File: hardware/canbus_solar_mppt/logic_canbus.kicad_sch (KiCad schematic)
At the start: 31 parts, among them J4 Conn_01x05_Male, J5 CANPWR, J6 CANGND, J7 RJ45, J8 RJ45, J9 Conn_02x03_Odd_Even, Q9 BSS123, U5 2.048V, U6 PIC18F27Q84, U7 TLE9250VSJXUMA1, Y1 10Mhz

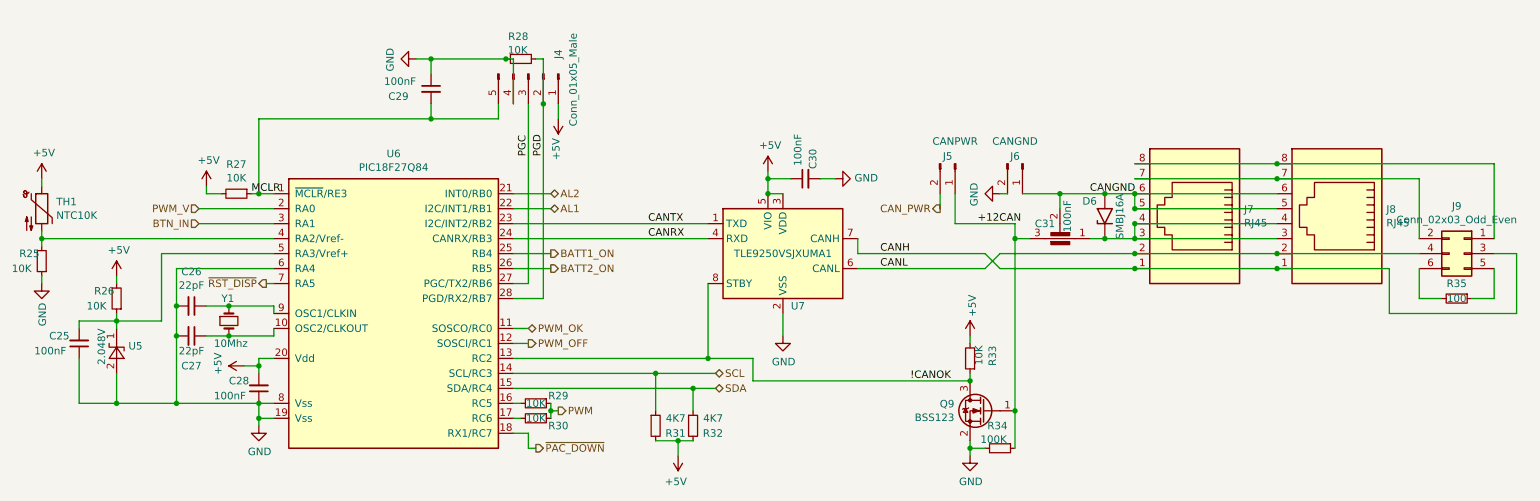
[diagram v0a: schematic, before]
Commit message: Switch from BSS123 + GS resistor to DGD0215 mosfet driver.
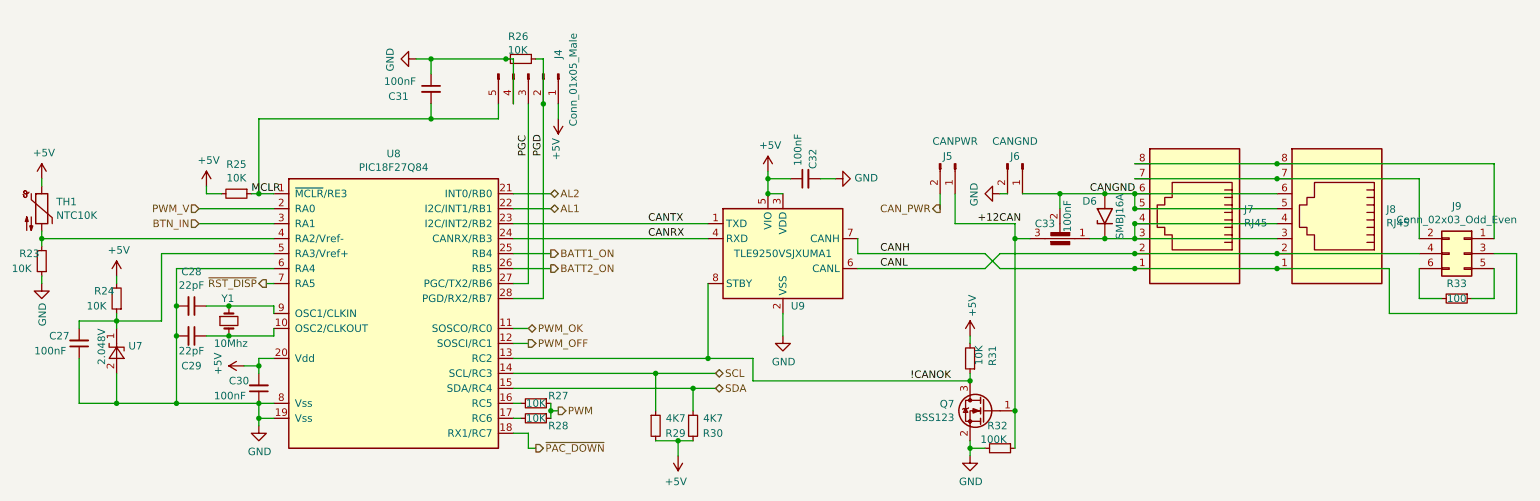
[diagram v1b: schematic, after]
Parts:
- renumbered C25 to C27, C26 to C28, C27 to C29, C28 to C30, C29 to C31, C30 to C32, C31 to C33, Q9 to Q7, R25 to R23, R26 to R24, R27 to R25, R28 to R26, R29 to R27, R30 to R28, R31 to R29, R32 to R30, R33 to R31, R34 to R32, R35 to R33, U5 to U7, U6 to U8, U7 to U9
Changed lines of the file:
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@@
   (symbol (lib_id "Device:Q_NMOS_GSD") (at 191.77 109.22 0) (mirror y) (unit 1)
     (in_bom yes) (on_board yes)
-    (property "Reference" "Q9" (id 0) (at 186.563 108.0516 0)
+    (property "Reference" "Q7" (id 0) (at 186.563 108.0516 0)
       (effects (font (size 1.27 1.27)) (justify left))
     )
@@
   (symbol (lib_id "Device:C_Small") (at 68.58 105.41 180) (unit 1)
     (in_bom yes) (on_board yes)
-    (property "Reference" "C28" (id 0) (at 63.5 104.14 0)
+    (property "Reference" "C30" (id 0) (at 63.5 104.14 0)
       (effects (font (size 1.27 1.27)) (justify right))
     )
@@
   (symbol (lib_id "Device:R_Small") (at 113.03 49.53 270) (unit 1)
     (in_bom yes) (on_board yes)
-    (property "Reference" "R28" (id 0) (at 114.3 45.72 90)
+    (property "Reference" "R26" (id 0) (at 114.3 45.72 90)
       (effects (font (size 1.27 1.27)) (justify right))
     )
@@
   (symbol (lib_id "Device:C_Feedthrough") (at 204.47 77.47 180) (unit 1)
     (in_bom yes) (on_board yes)
-    (property "Reference" "C31" (id 0) (at 201.93 77.47 0))
+    (property "Reference" "C33" (id 0) (at 201.93 77.47 0))
     (property "Value" "100nF" (id 1) (at 205.74 76.2 90))
     (property "Footprint" "local:C_filter_0805" (id 2) (at 204.47 77.47 90)
@@
   (symbol (lib_id "Device:C_Small") (at 97.79 54.61 0) (unit 1)
     (in_bom yes) (on_board yes)
-    (property "Reference" "C29" (id 0) (at 93.98 55.88 0)
+    (property "Reference" "C31" (id 0) (at 93.98 55.88 0)
       (effects (font (size 1.27 1.27)) (justify right))
     )
@@
   (symbol (lib_id "microchip-local:PIC18F27Q84") (at 91.44 92.71 0) (unit 1)
     (in_bom yes) (on_board yes)
-    (property "Reference" "U6" (id 0) (at 91.44 65.6082 0))
+    (property "Reference" "U8" (id 0) (at 91.44 65.6082 0))
     (property "Value" "PIC18F27Q84" (id 1) (at 91.44 67.9196 0))
     (property "Footprint" "Package_SO:SOIC-28W_7.5x17.9mm_P1.27mm" (id 2) (at 91.44 99.06 0)
@@
   (symbol (lib_id "Device:C_Small") (at 38.1 97.79 180) (unit 1)
     (in_bom yes) (on_board yes)
-    (property "Reference" "C25" (id 0) (at 33.02 96.52 0)
+    (property "Reference" "C27" (id 0) (at 33.02 96.52 0)
       (effects (font (size 1.27 1.27)) (justify right))
     )
@@
   (symbol (lib_id "Device:C_Small") (at 161.29 69.85 90) (unit 1)
     (in_bom yes) (on_board yes)
-    (property "Reference" "C30" (id 0) (at 162.56 64.77 0)
+    (property "Reference" "C32" (id 0) (at 162.56 64.77 0)
       (effects (font (size 1.27 1.27)) (justify right))
     )
@@
   (symbol (lib_id "Device:R_Small") (at 194.31 115.57 270) (unit 1)
     (in_bom yes) (on_board yes)
-    (property "Reference" "R34" (id 0) (at 195.58 111.76 90)
+    (property "Reference" "R32" (id 0) (at 195.58 111.76 90)
       (effects (font (size 1.27 1.27)) (justify right))
     )
@@
   (symbol (lib_id "Device:R_Small") (at 64.77 72.39 270) (unit 1)
     (in_bom yes) (on_board yes)
-    (property "Reference" "R27" (id 0) (at 64.77 67.4116 90))
+    (property "Reference" "R25" (id 0) (at 64.77 67.4116 90))
     (property "Value" "10K" (id 1) (at 64.77 69.723 90))
     (property "Footprint" "Resistor_SMD:R_0805_2012Metric_Pad1.20x1.40mm_HandSolder" (id 2) (at 64.77 72.39 0)
@@
   (symbol (lib_id "Device:R_Small") (at 115.57 110.49 270) (unit 1)
     (in_bom yes) (on_board yes)
-    (property "Reference" "R30" (id 0) (at 119.38 111.76 90))
+    (property "Reference" "R28" (id 0) (at 119.38 111.76 90))
     (property "Value" "10K" (id 1) (at 115.57 110.49 90))
     (property "Footprint" "Resistor_SMD:R_0805_2012Metric_Pad1.20x1.40mm_HandSolder" (id 2) (at 115.57 110.49 0)
@@
   (symbol (lib_id "Interface_CAN_LIN:MCP2542FDxMF") (at 157.48 82.55 0) (unit 1)
     (in_bom yes) (on_board yes)
-    (property "Reference" "U7" (id 0) (at 160.02 91.44 0))
+    (property "Reference" "U9" (id 0) (at 160.02 91.44 0))
     (property "Value" "TLE9250VSJXUMA1" (id 1) (at 157.48 82.55 0))
     (property "Footprint" "Package_SO:SOIC-8_3.9x4.9mm_P1.27mm" (id 2) (at 157.48 95.25 0)
@@
   (symbol (lib_id "Device:R_Small") (at 44.45 90.17 180) (unit 1)
     (in_bom yes) (on_board yes)
-    (property "Reference" "R26" (id 0) (at 40.64 88.9 0)
+    (property "Reference" "R24" (id 0) (at 40.64 88.9 0)
       (effects (font (size 1.27 1.27)) (justify right))
     )
@@
   (symbol (lib_id "Device:R_Small") (at 135.89 111.76 0) (unit 1)
     (in_bom yes) (on_board yes)
-    (property "Reference" "R31" (id 0) (at 140.97 113.03 0)
+    (property "Reference" "R29" (id 0) (at 140.97 113.03 0)
       (effects (font (size 1.27 1.27)) (justify right))
     )
@@
   (symbol (lib_id "Device:C_Small") (at 57.15 96.52 270) (unit 1)
     (in_bom yes) (on_board yes)
-    (property "Reference" "C27" (id 0) (at 57.15 101.6 90))
+    (property "Reference" "C29" (id 0) (at 57.15 101.6 90))
     (property "Value" "22pF" (id 1) (at 57.15 99.06 90))
     (property "Footprint" "Capacitor_THT:C_Disc_D3.8mm_W2.6mm_P2.50mm" (id 2) (at 57.15 96.52 0)
@@
   (symbol (lib_id "Device:R_Small") (at 31.75 83.82 180) (unit 1)
     (in_bom yes) (on_board yes)
-    (property "Reference" "R25" (id 0) (at 27.94 82.55 0)
+    (property "Reference" "R23" (id 0) (at 27.94 82.55 0)
       (effects (font (size 1.27 1.27)) (justify right))
     )
@@
   (symbol (lib_id "Device:R_Small") (at 115.57 107.95 270) (unit 1)
     (in_bom yes) (on_board yes)
-    (property "Reference" "R29" (id 0) (at 119.38 106.68 90))
+    (property "Reference" "R27" (id 0) (at 119.38 106.68 90))
     (property "Value" "10K" (id 1) (at 115.57 107.95 90))
     (property "Footprint" "Resistor_SMD:R_0805_2012Metric_Pad1.20x1.40mm_HandSolder" (id 2) (at 115.57 107.95 0)
@@
   (symbol (lib_id "Device:R_Small") (at 271.78 90.17 270) (unit 1)
     (in_bom yes) (on_board yes)
-    (property "Reference" "R35" (id 0) (at 271.78 87.63 90))
+    (property "Reference" "R33" (id 0) (at 271.78 87.63 90))
     (property "Value" "100" (id 1) (at 271.78 90.17 90))
     (property "Footprint" "Resistor_SMD:R_0805_2012Metric_Pad1.20x1.40mm_HandSolder" (id 2) (at 271.78 90.17 0)
@@
   (symbol (lib_id "Device:R_Small") (at 189.23 100.33 180) (unit 1)
     (in_bom yes) (on_board yes)
-    (property "Reference" "R33" (id 0) (at 193.04 101.6 90)
+    (property "Reference" "R31" (id 0) (at 193.04 101.6 90)
       (effects (font (size 1.27 1.27)) (justify right))
     )
@@
   (symbol (lib_id "Device:C_Small") (at 57.15 91.44 270) (unit 1)
     (in_bom yes) (on_board yes)
-    (property "Reference" "C26" (id 0) (at 57.15 85.6234 90))
+    (property "Reference" "C28" (id 0) (at 57.15 85.6234 90))
     (property "Value" "22pF" (id 1) (at 57.15 87.9348 90))
     (property "Footprint" "Capacitor_THT:C_Disc_D3.8mm_W2.6mm_P2.50mm" (id 2) (at 57.15 91.44 0)
@@
   (symbol (lib_id "Reference_Voltage:LM4040DBZ-2.0") (at 44.45 99.06 90) (unit 1)
     (in_bom yes) (on_board yes)
-    (property "Reference" "U5" (id 0) (at 46.4566 98.2253 90)
+    (property "Reference" "U7" (id 0) (at 46.4566 98.2253 90)
       (effects (font (size 1.27 1.27)) (justify right))
     )
@@
   (symbol (lib_id "Device:R_Small") (at 142.24 111.76 0) (unit 1)
     (in_bom yes) (on_board yes)
-    (property "Reference" "R32" (id 0) (at 147.32 113.03 0)
-      (effects (font (size 1.27 1.27)) (justify right))
-    )
+    (property "Reference" "R30" (id 0) (at 147.32 113.03 0)
+      (effects (font (size 1.27 1.27)) (justify right))
+    )
